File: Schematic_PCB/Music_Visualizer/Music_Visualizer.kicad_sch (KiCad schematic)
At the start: 130 parts, among them J1 AudioJack2_Ground, SW1 SW_SPDT, U1 LM324, U2 LM324, U3 LM324, U4 LM324, U5 LM324, U6 LM324

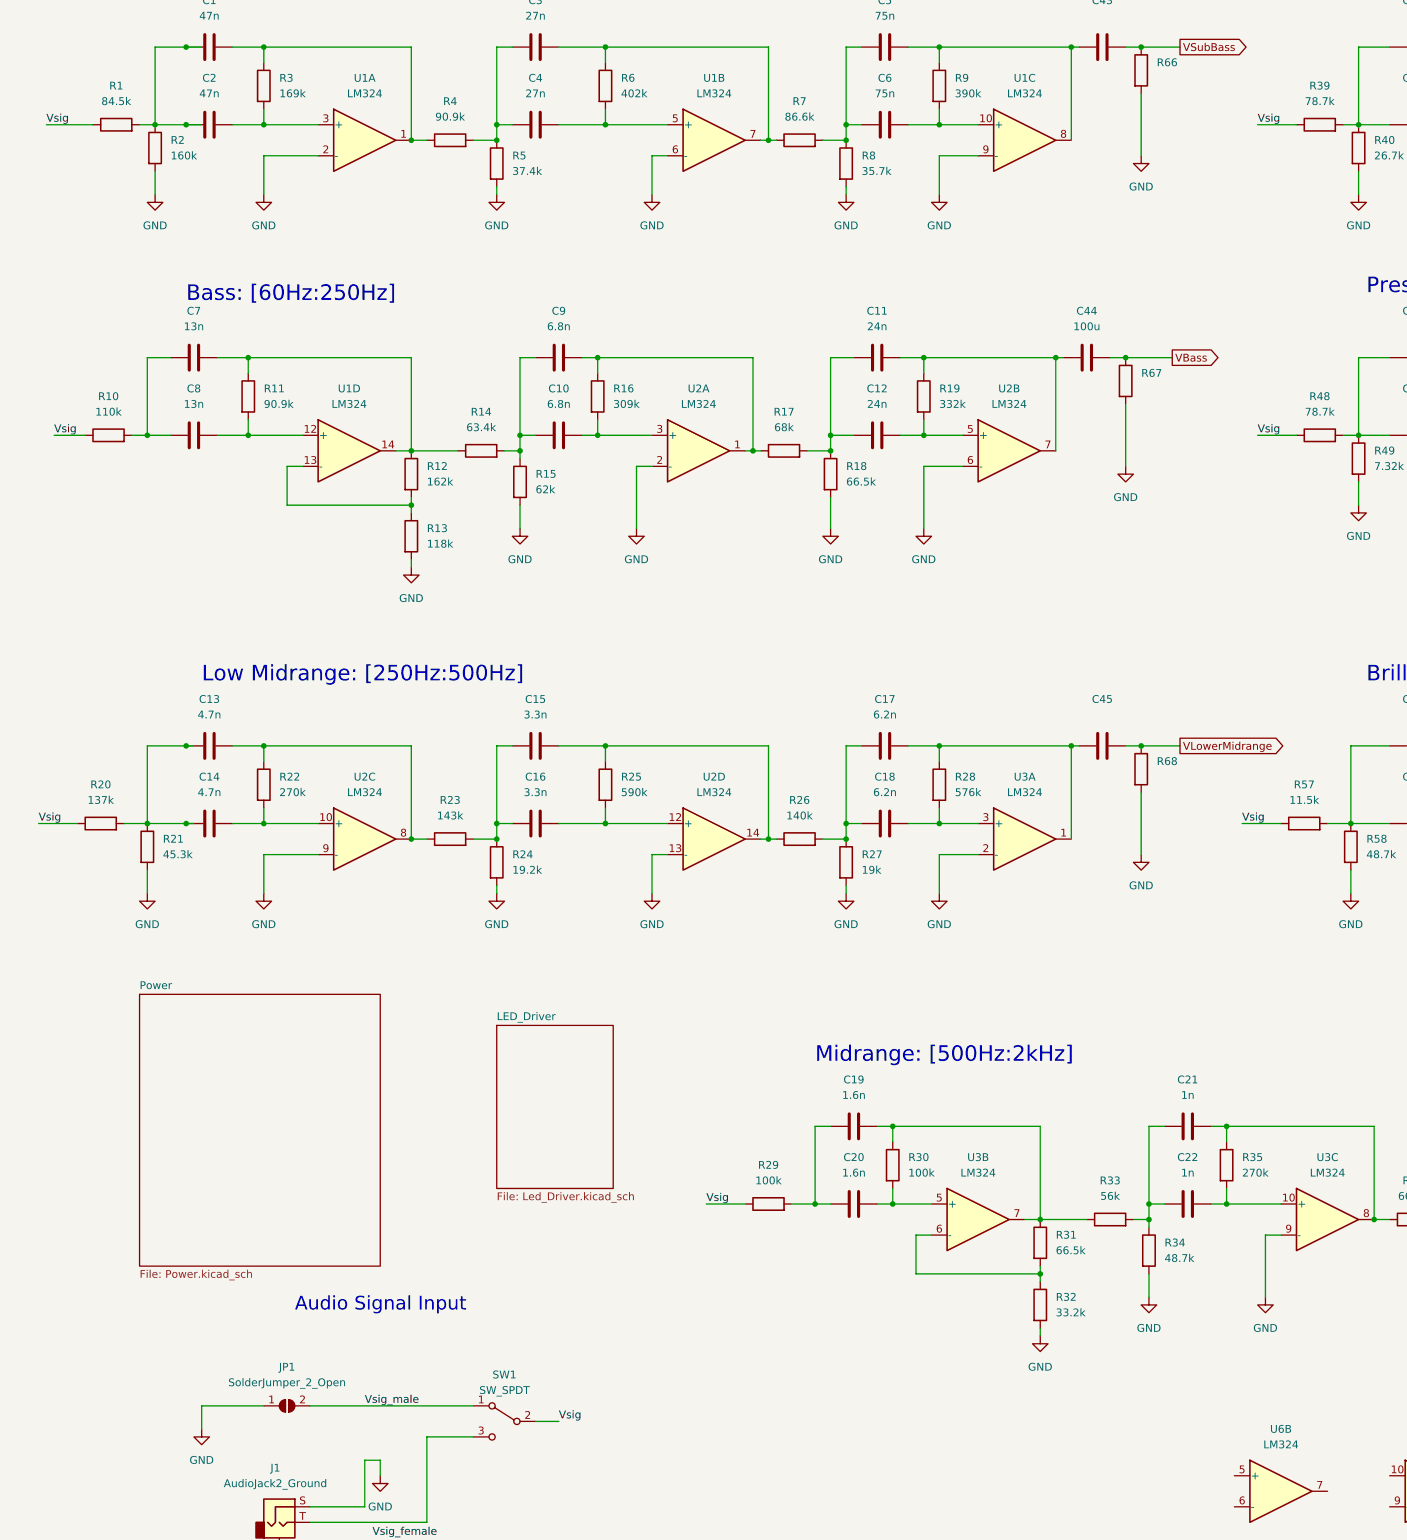
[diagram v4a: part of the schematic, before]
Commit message: Used Global labels
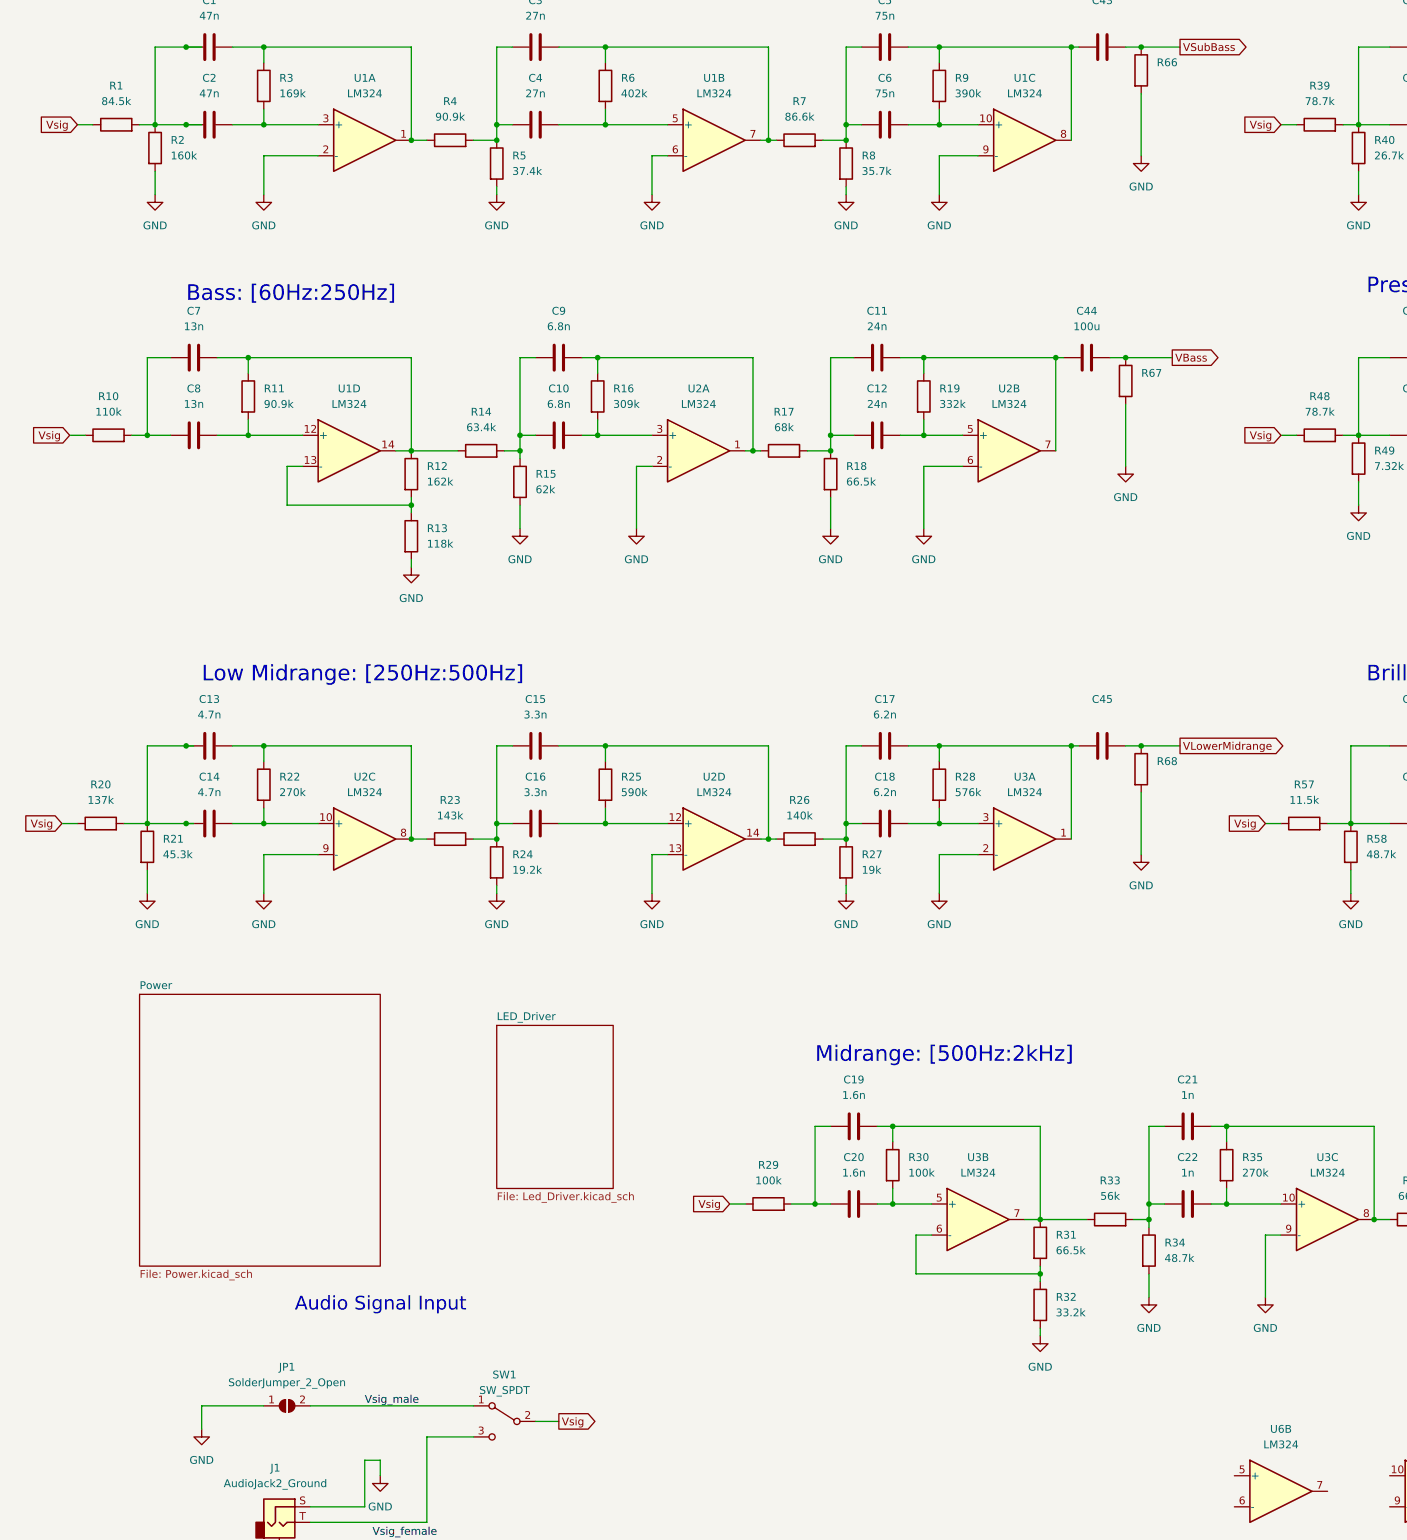
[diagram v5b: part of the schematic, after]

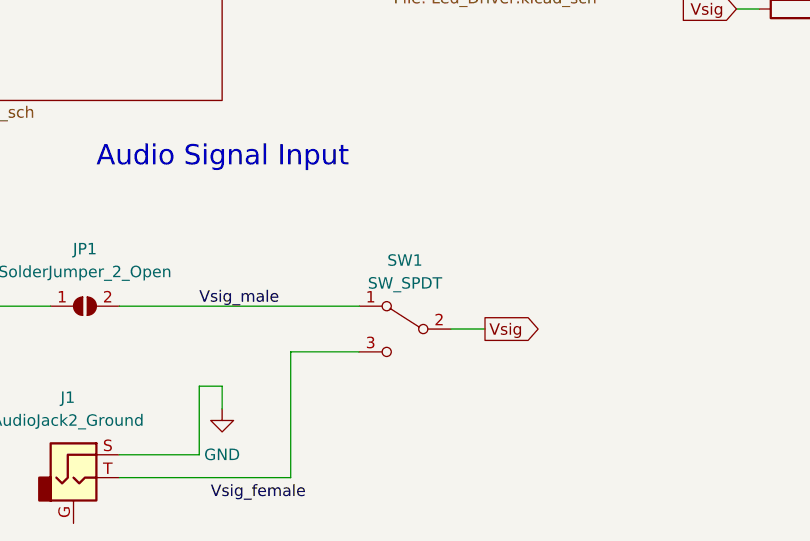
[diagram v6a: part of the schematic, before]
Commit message: Organized all subcircuits in PCB editor
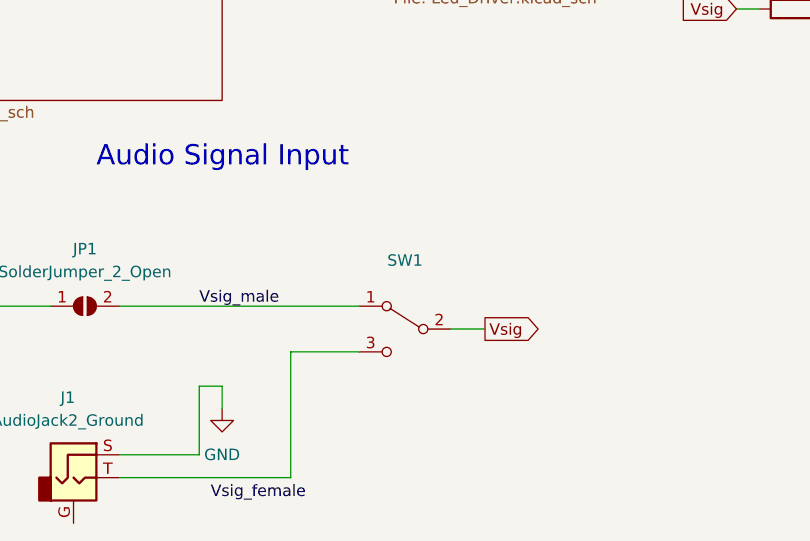
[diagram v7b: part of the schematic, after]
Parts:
- SW1: value SW_SPDT -> (none); footprint local:SW_OS102011MS2QN1 -> (none)
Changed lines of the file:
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@@
     (in_bom yes) (on_board yes) (fields_autoplaced)
     (property "Reference" "SW1" (id 0) (at 91.44 251.46 0))
-    (property "Value" "SW_SPDT" (id 1) (at 91.44 254 0))
-    (property "Footprint" "local:SW_OS102011MS2QN1" (id 2) (at 91.44 259.08 0)
+    (property "Value" "" (id 1) (at 91.44 254 0))
+    (property "Footprint" "" (id 2) (at 91.44 259.08 0)
       (effects (font (size 1.27 1.27)) hide)
     )
@@
       (reference "#PWR0101") (unit 1) (value "GND") (footprint "")
     )
+    (path "/56ed3a67-eed8-4688-8767-d6bf63bd87ca/a2358d1e-6b27-4973-acba-fcd63cd710b2"
+      (reference "#PWR?") (unit 1) (value "GND") (footprint "")
+    )
+    (path "/56ed3a67-eed8-4688-8767-d6bf63bd87ca/f9251750-1ec8-4b28-94a2-e2c2fd034a76"
+      (reference "#PWR?") (unit 1) (value "GND") (footprint "")
+    )
     (path "/d3791e18-fb94-4a94-9f9d-30d4fd98db8e"
       (reference "C1") (unit 1) (value "47n") (footprint "Capacitor_SMD:C_0201_0603Metric")
@@
       (reference "C57") (unit 1) (value "220u") (footprint "Capacitor_THT:CP_Radial_D6.3mm_P2.50mm")
     )
+    (path "/56ed3a67-eed8-4688-8767-d6bf63bd87ca/0c400b59-f5ad-4850-a5d0-92cb04b649a3"
+      (reference "C58") (unit 1) (value "1u") (footprint "Capacitor_SMD:C_0402_1005Metric")
+    )
+    (path "/56ed3a67-eed8-4688-8767-d6bf63bd87ca/694ebbfc-d42f-4b27-9ff7-8a84762b2961"
+      (reference "C59") (unit 1) (value "1u") (footprint "Capacitor_SMD:C_0402_1005Metric")
+    )
     (path "/56ed3a67-eed8-4688-8767-d6bf63bd87ca/de358774-c2e9-4344-b111-e849f00e8b6c"
       (reference "D1") (unit 1) (value "LED") (footprint "LED_THT:LED_D5.0mm")
@@
     )
     (path "/f3e6156e-7d01-4597-b7d3-9fd9cf393cea"
-      (reference "SW1") (unit 1) (value "SW_SPDT") (footprint "local:SW_OS102011MS2QN1")
+      (reference "SW1") (unit 1) (value "SW_SPDT") (footprint "Slide_Switch:SW_OS102011MS2QN1")
     )
     (path "/7a70fb5f-edf3-42ca-8da4-fb415c6f3b93"
